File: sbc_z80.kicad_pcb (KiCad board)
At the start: 4 copper layers, 101.6 x 50.8 mm, 72 parts, among them J1 RC80 Bus, J2 UPDI TTL, J3 PIO Header, J4 Conn_01x06, J5 Conn_01x06, J6 CTC Header, J7 AVR-JTAG-10, SW1 SW_Push, SW2 SW_DIP_x06, U1 CPU - Z84C0010AEG, U10 74HC04, U11 ATtiny1614-SS, U12 MIC811LUY, U13 AS1115-BSST, U14 ACDA02-41SGWA-F01, U2 TPS7A0533PDBVR, U3 SRAM - IS62C5128BL-45TLI, U4 GLS29EE010, U5 Si5351A-B-GT, U6 SIO/3 - Z84C4310AEG, U7 CPLD - EPM7032STC44, U8 CTC - Z84C3010AEG, U9 PIO - Z84C2010AEG, Y1 25MHZ 8PF

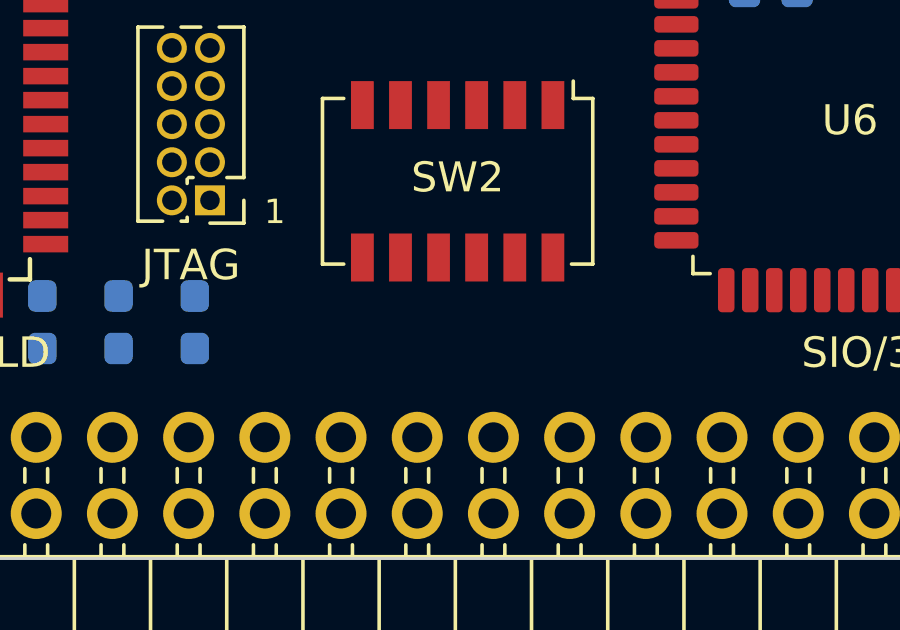
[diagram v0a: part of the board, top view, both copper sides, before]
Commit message: fixed NC pins
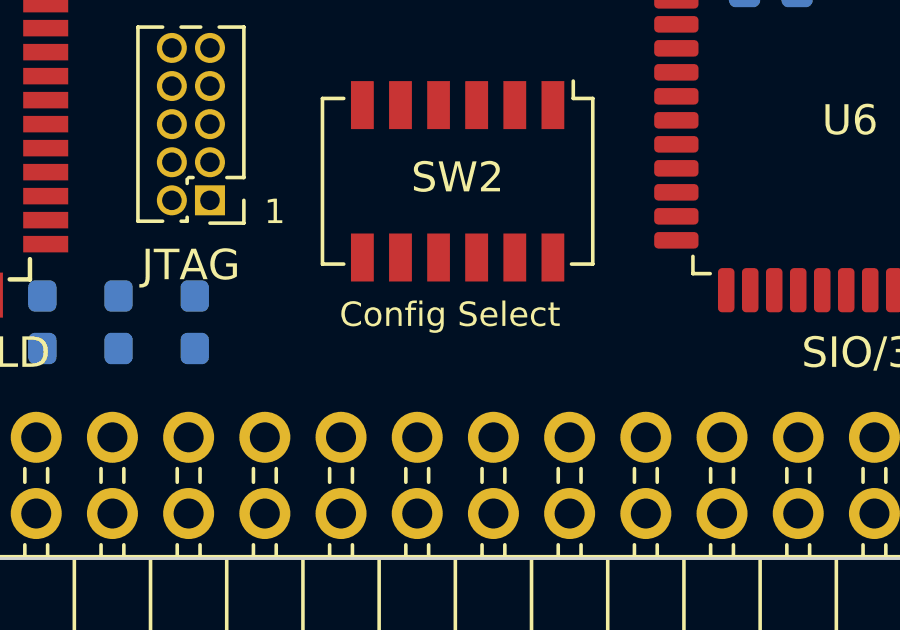
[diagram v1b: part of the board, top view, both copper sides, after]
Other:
- board text added: "Config Select"
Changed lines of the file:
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@@
   (general
     (thickness 1.6)
-    (drawings 37)
+    (drawings 38)
     (tracks 0)
     (zones 0)
@@
     (add_net /A17)
     (add_net /A18)
-    (add_net /A19)
     (add_net /A2)
-    (add_net /A20)
-    (add_net /A21)
-    (add_net /A22)
-    (add_net /A23)
     (add_net /A3)
     (add_net /A4)
@@
     (add_net /BRDY)
     (add_net /CLK)
-    (add_net /CLK2)
-    (add_net /CLKX)
     (add_net /CLK_F)
     (add_net /CLK_U)
@@
     (add_net /D0)
     (add_net /D1)
-    (add_net /D10)
-    (add_net /D11)
-    (add_net /D12)
-    (add_net /D13)
-    (add_net /D14)
-    (add_net /D15)
     (add_net /D2)
     (add_net /D3)
@@
     (add_net /D6)
     (add_net /D7)
-    (add_net /D8)
-    (add_net /D9)
-    (add_net "/Display and Clocks/D_ENA")
     (add_net "/Display and Clocks/RX")
     (add_net "/Display and Clocks/SCL")
@@
     (add_net /TXA)
     (add_net /TXB)
-    (add_net /USR1)
-    (add_net /USR2)
-    (add_net /USR3)
-    (add_net /USR5)
-    (add_net /USR6)
-    (add_net /USR7)
     (add_net /ZT0)
     (add_net /ZT1)
     (add_net /ZT2)
-    (add_net /~A0)
     (add_net /~ASTB)
     (add_net /~BSTB)
@@
     (add_net /~CTSA)
     (add_net /~CTSB)
-    (add_net /~DIO)
     (add_net /~HALT)
     (add_net /~INT)
@@
     (add_net /~MREQ)
     (add_net /~NMI)
-    (add_net /~PAGE)
     (add_net /~PIO)
     (add_net /~RAM)
     (add_net /~RD)
     (add_net /~RESET)
-    (add_net /~RFSH)
     (add_net /~ROM)
     (add_net /~RTSA)
@@
     (add_net "Net-(D1-Pad3)")
     (add_net "Net-(D1-Pad4)")
-    (add_net "Net-(J1-Pad41)")
-    (add_net "Net-(J1-Pad42)")
-    (add_net "Net-(J1-Pad43)")
-    (add_net "Net-(J1-Pad44)")
-    (add_net "Net-(J1-Pad45)")
-    (add_net "Net-(J1-Pad46)")
-    (add_net "Net-(J1-Pad47)")
-    (add_net "Net-(J1-Pad48)")
     (add_net "Net-(J4-Pad2)")
-    (add_net "Net-(J4-Pad3)")
     (add_net "Net-(J4-Pad4)")
     (add_net "Net-(J4-Pad5)")
     (add_net "Net-(J4-Pad6)")
     (add_net "Net-(J5-Pad2)")
-    (add_net "Net-(J5-Pad3)")
     (add_net "Net-(J5-Pad4)")
     (add_net "Net-(J5-Pad5)")
     (add_net "Net-(J5-Pad6)")
-    (add_net "Net-(J7-Pad7)")
-    (add_net "Net-(J7-Pad8)")
     (add_net "Net-(R22-Pad1)")
     (add_net "Net-(R4-Pad2)")
     (add_net "Net-(SW1-Pad2)")
-    (add_net "Net-(SW2-Pad1)")
-    (add_net "Net-(SW2-Pad10)")
-    (add_net "Net-(SW2-Pad11)")
-    (add_net "Net-(SW2-Pad12)")
-    (add_net "Net-(SW2-Pad2)")
-    (add_net "Net-(SW2-Pad3)")
-    (add_net "Net-(SW2-Pad4)")
-    (add_net "Net-(SW2-Pad5)")
-    (add_net "Net-(SW2-Pad6)")
-    (add_net "Net-(SW2-Pad7)")
-    (add_net "Net-(SW2-Pad8)")
-    (add_net "Net-(SW2-Pad9)")
     (add_net "Net-(U1-Pad11)")
-    (add_net "Net-(U1-Pad25)")
     (add_net "Net-(U10-Pad1)")
-    (add_net "Net-(U10-Pad12)")
     (add_net "Net-(U10-Pad3)")
     (add_net "Net-(U10-Pad5)")
-    (add_net "Net-(U13-Pad1)")
-    (add_net "Net-(U13-Pad10)")
-    (add_net "Net-(U13-Pad11)")
-    (add_net "Net-(U13-Pad12)")
-    (add_net "Net-(U13-Pad13)")
-    (add_net "Net-(U13-Pad14)")
-    (add_net "Net-(U13-Pad15)")
-    (add_net "Net-(U13-Pad16)")
-    (add_net "Net-(U13-Pad17)")
-    (add_net "Net-(U13-Pad18)")
-    (add_net "Net-(U13-Pad19)")
-    (add_net "Net-(U13-Pad2)")
-    (add_net "Net-(U13-Pad20)")
-    (add_net "Net-(U13-Pad21)")
-    (add_net "Net-(U13-Pad22)")
-    (add_net "Net-(U13-Pad23)")
-    (add_net "Net-(U13-Pad24)")
-    (add_net "Net-(U13-Pad3)")
-    (add_net "Net-(U13-Pad4)")
-    (add_net "Net-(U13-Pad5)")
-    (add_net "Net-(U13-Pad6)")
-    (add_net "Net-(U13-Pad7)")
-    (add_net "Net-(U13-Pad8)")
-    (add_net "Net-(U13-Pad9)")
-    (add_net "Net-(U14-Pad1)")
-    (add_net "Net-(U14-Pad10)")
-    (add_net "Net-(U14-Pad11)")
-    (add_net "Net-(U14-Pad12)")
-    (add_net "Net-(U14-Pad13)")
-    (add_net "Net-(U14-Pad14)")
-    (add_net "Net-(U14-Pad15)")
-    (add_net "Net-(U14-Pad16)")
-    (add_net "Net-(U14-Pad17)")
-    (add_net "Net-(U14-Pad18)")
-    (add_net "Net-(U14-Pad19)")
-    (add_net "Net-(U14-Pad2)")
-    (add_net "Net-(U14-Pad20)")
-    (add_net "Net-(U14-Pad3)")
-    (add_net "Net-(U14-Pad4)")
-    (add_net "Net-(U14-Pad5)")
-    (add_net "Net-(U14-Pad6)")
-    (add_net "Net-(U14-Pad7)")
-    (add_net "Net-(U14-Pad8)")
-    (add_net "Net-(U14-Pad9)")
-    (add_net "Net-(U2-Pad4)")
     (add_net "Net-(U4-Pad1)")
     (add_net "Net-(U5-Pad2)")
     (add_net "Net-(U5-Pad3)")
-    (add_net "Net-(U6-Pad1)")
-    (add_net "Net-(U6-Pad10)")
-    (add_net "Net-(U6-Pad15)")
-    (add_net "Net-(U6-Pad16)")
     (add_net "Net-(U6-Pad17)")
-    (add_net "Net-(U6-Pad38)")
-    (add_net "Net-(U6-Pad40)")
-    (add_net "Net-(U7-Pad18)")
-    (add_net "Net-(U7-Pad19)")
-    (add_net "Net-(U7-Pad20)")
-    (add_net "Net-(U7-Pad21)")
-    (add_net "Net-(U7-Pad22)")
-    (add_net "Net-(U7-Pad23)")
-    (add_net "Net-(U7-Pad25)")
-    (add_net "Net-(U7-Pad38)")
-    (add_net "Net-(U7-Pad39)")
-    (add_net "Net-(U7-Pad40)")
     (add_net "Net-(U8-Pad11)")
     (add_net "Net-(U9-Pad2)")
@@
     )
   )
+  (gr_text "Config Select" (at 148.971 119.38) (layer F.SilkS)
+    (effects (font (size 0.8128 0.8128) (thickness 0.1524)))
+  )
   (gr_text THS-80 (at 95.504 102.87) (layer F.SilkS)

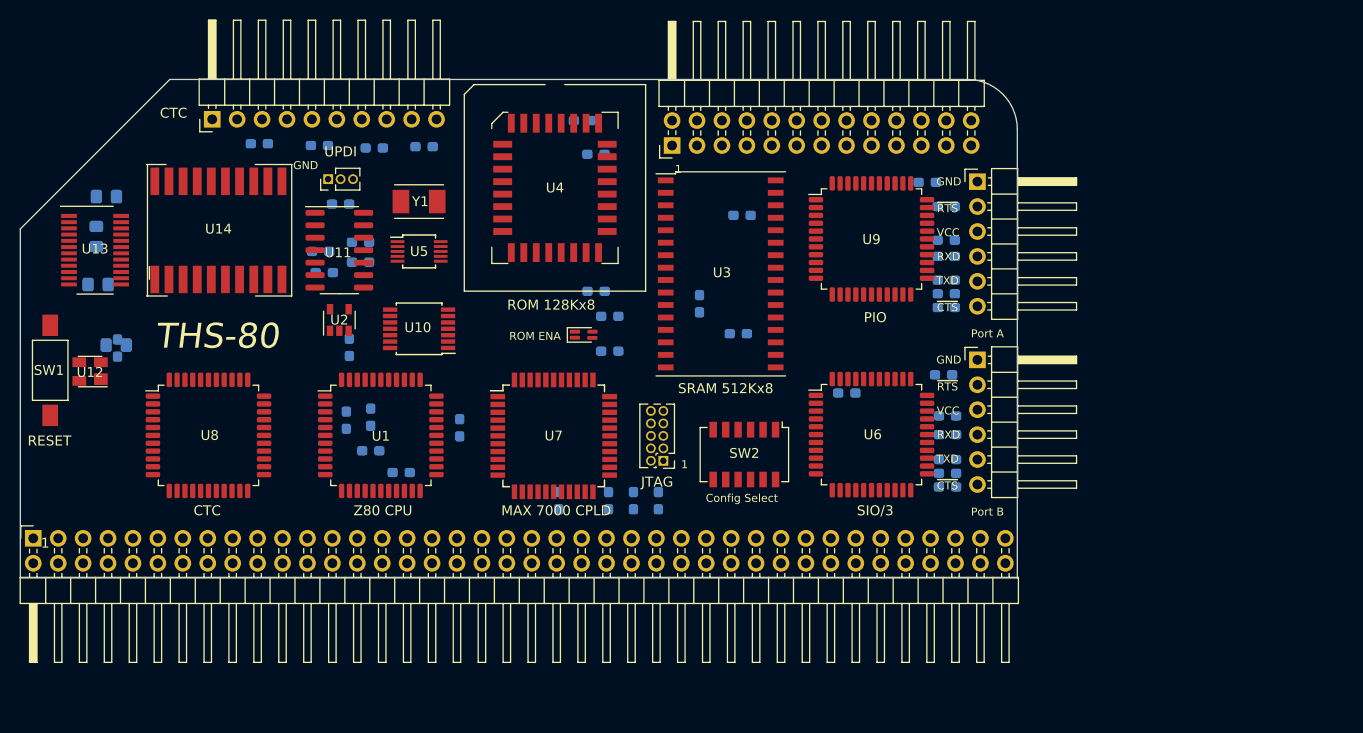
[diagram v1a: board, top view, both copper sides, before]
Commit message: changed part layout, removed switch
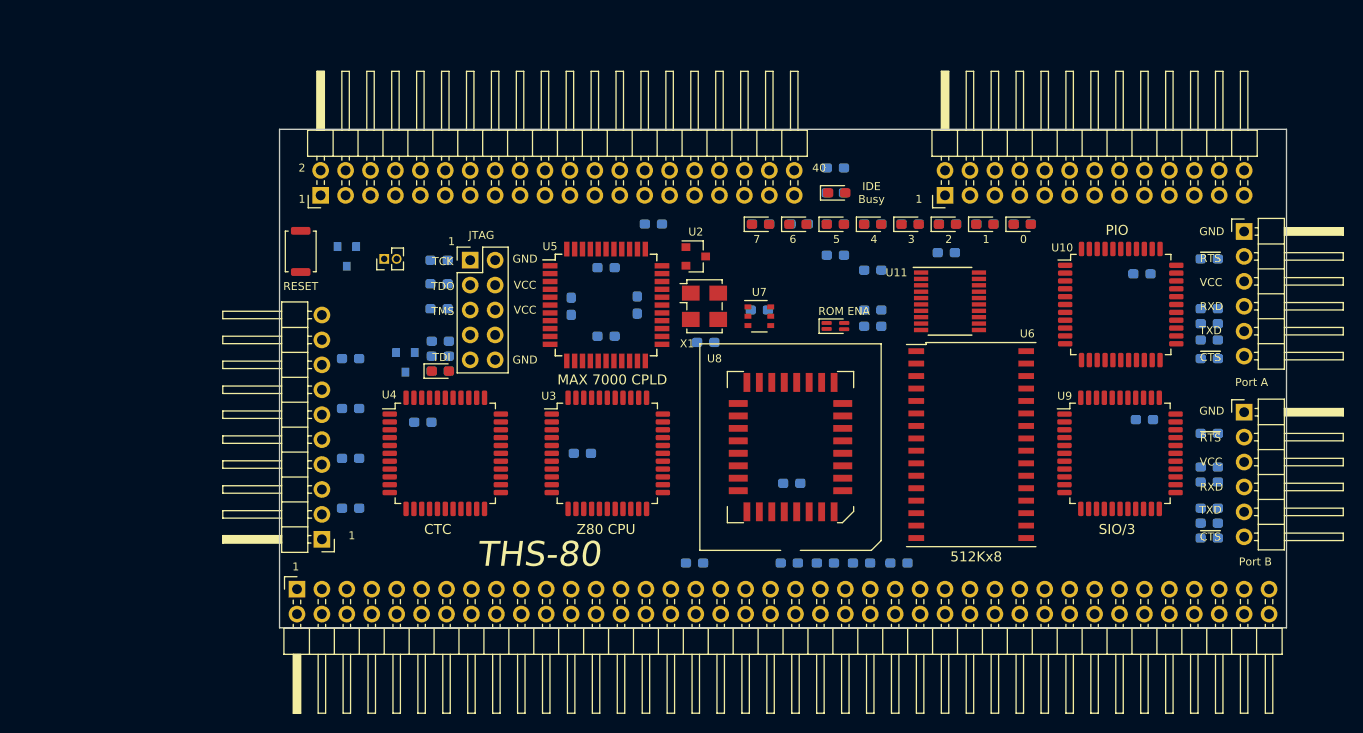
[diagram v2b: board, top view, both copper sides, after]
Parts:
- removed the C1 at (83.2, 92.7)
- removed C15, C16: 0.47uF, Capacitor_SMD:C_0603_1608Metric_Pad1.05x0.95mm_HandSolder
- removed the C2 at (84.2, 88.6)
- removed the C3 at (83.4, 97.6)
- removed the C4 at (85.2, 103.8)
- removed the J5 at (173.0, 105.3)
- removed the R26 at (105.9, 83.4)
- removed the R28 at (116.6, 83.6)
- removed the SW1 at (78.5, 106.3)
- removed U13: AS1115-BSST, Package_SO:QSOP-24_3.9x8.7mm_P0.635mm
- removed U14: ACDA02-41SGWA-F01, Display:ACDA02-41SGWA-F01
- removed the U2 at (108.0, 101.2)
- removed the U4 at (129.9, 87.8)
- removed the U5 at (116.1, 94.2)
- removed Y1: 25MHZ 8PF, Crystal:Crystal_SMD_TXC_7A-2Pin_5x3.2mm
- added C11: 100nF, Capacitor_SMD:C_0603_1608Metric_Pad1.05x0.95mm_HandSolder, B.Cu at (144.1, 126.0)
- added D10: Green, LED_SMD:LED_0603_1608Metric_Pad1.05x0.95mm_HandSolder, F.Cu at (154.7, 91.5)
- added D11: Green, LED_SMD:LED_0603_1608Metric_Pad1.05x0.95mm_HandSolder, F.Cu at (150.9, 91.5)
- added D2: LED, LED_SMD:LED_0603_1608Metric_Pad1.05x0.95mm_HandSolder, F.Cu at (158.6, 88.3)
- added D3: Red/Green, LED_SMD:LED_2C_0603_1608Metric_Pad1.05x0.95mm_HandSolder, F.Cu at (158.5, 101.9)
- added D4: Green, LED_SMD:LED_0603_1608Metric_Pad1.05x0.95mm_HandSolder, F.Cu at (177.5, 91.5)
- added D5: Green, LED_SMD:LED_0603_1608Metric_Pad1.05x0.95mm_HandSolder, F.Cu at (173.7, 91.5)
- added D6: Green, LED_SMD:LED_0603_1608Metric_Pad1.05x0.95mm_HandSolder, F.Cu at (169.9, 91.5)
- added D7: Green, LED_SMD:LED_0603_1608Metric_Pad1.05x0.95mm_HandSolder, F.Cu at (166.1, 91.5)
- added D8: Green, LED_SMD:LED_0603_1608Metric_Pad1.05x0.95mm_HandSolder, F.Cu at (162.3, 91.5)
- added D9: Green, LED_SMD:LED_0603_1608Metric_Pad1.05x0.95mm_HandSolder, F.Cu at (158.5, 91.5)
- added J3: AVR-JTAG-10, Connector_PinHeader_2.54mm:PinHeader_2x05_P2.54mm_Vertical, F.Cu at (121.3, 95.1)
- added JP1: Jumper_NC_Small, Connector_PinHeader_1.27mm:PinHeader_1x02_P1.27mm_Vertical, F.Cu at (112.5, 95.0)
- added Q1: IRLML6402, Package_TO_SOT_SMD:SOT-23, B.Cu at (114.7, 105.5)
- added R29: 680R, Resistor_SMD:R_0603_1608Metric_Pad1.05x0.95mm_HandSolder, B.Cu at (154.8, 91.4)
- added R30: 680R, Resistor_SMD:R_0603_1608Metric_Pad1.05x0.95mm_HandSolder, B.Cu at (150.9, 91.4)
- added R35: 2K2, Resistor_SMD:R_0603_1608Metric_Pad1.05x0.95mm_HandSolder, B.Cu at (196.6, 112.8)
- added R36: 2K2, Resistor_SMD:R_0603_1608Metric_Pad1.05x0.95mm_HandSolder, B.Cu at (196.6, 117.7)
- added R37: 2K2, Resistor_SMD:R_0603_1608Metric_Pad1.05x0.95mm_HandSolder, B.Cu at (196.6, 120.4)
- added R38: 2K2, Resistor_SMD:R_0603_1608Metric_Pad1.05x0.95mm_HandSolder, B.Cu at (196.6, 123.4)
- added R39: 100K, Resistor_SMD:R_0603_1608Metric_Pad1.05x0.95mm_HandSolder, B.Cu at (196.6, 101.6)
- added R40: 100K, Resistor_SMD:R_0603_1608Metric_Pad1.05x0.95mm_HandSolder, B.Cu at (196.6, 116.2)
- added R41: 100K, Resistor_SMD:R_0603_1608Metric_Pad1.05x0.95mm_HandSolder, B.Cu at (162.3, 96.1)
- added R42: 100K, Resistor_SMD:R_0603_1608Metric_Pad1.05x0.95mm_HandSolder, B.Cu at (196.6, 121.9)
- added R6: 10K, Resistor_SMD:R_0603_1608Metric_Pad1.05x0.95mm_HandSolder, B.Cu at (109.1, 115.3)
- added R7: 10K, Resistor_SMD:R_0603_1608Metric_Pad1.05x0.95mm_HandSolder, B.Cu at (109.1, 110.2)
- added R8: 10K, Resistor_SMD:R_0603_1608Metric_Pad1.05x0.95mm_HandSolder, B.Cu at (109.1, 105.2)
- added R9: 10K, Resistor_SMD:R_0603_1608Metric_Pad1.05x0.95mm_HandSolder, B.Cu at (109.1, 120.4)
- added U10: Z84C2010AEG, Package_QFP:LQFP-44_10x10mm_P0.8mm, F.Cu at (187.6, 99.6)
- added U6: SRAM - IS62C5128BL-45TLI, Package_SO:TSOP-II-32_21.0x10.2mm_P1.27mm, F.Cu at (172.3, 113.9)
- added X1: CTX-636 50mhz, Oscillator:Oscillator_SMD_TXC_7C-4Pin_5.0x3.2mm_HandSoldering, F.Cu at (145.2, 99.8)
- C7: renamed from C11; value 100nF -> 2.2uF
- D1: value Red/Green -> Green; footprint LED_SMD:LED_2C_0603_1608Metric_Pad1.05x0.95mm_HandSolder -> LED_SMD:LED_0603_1608Metric_Pad1.05x0.95mm_HandSolder
- J1: renamed from J4; value Conn_01x06 -> RC80 Bus; footprint Connector_PinHeader_2.54mm:PinHeader_1x06_P2.54mm_Horizontal -> Connector_PinHeader_2.54mm:PinHeader_2x40_Top_Bottom_P2.54mm_Horizontal
- J2: value UPDI TTL -> CTC Header; footprint Connector_PinHeader_1.27mm:PinHeader_1x03_P1.27mm_Vertical -> Connector_PinHeader_2.54mm:PinHeader_1x10_P2.54mm_Horizontal
- J4: renamed from J1; value RC80 Bus -> IDE; footprint Connector_PinHeader_2.54mm:PinHeader_2x40_Top_Bottom_P2.54mm_Horizontal -> Connector_PinHeader_2.54mm:PinHeader_2x20_P2.54mm_Horizontal
- J6: value CTC Header -> Conn_01x06; footprint Connector_PinHeader_2.54mm:PinHeader_1x10_P2.54mm_Horizontal -> Connector_PinHeader_2.54mm:PinHeader_1x06_P2.54mm_Horizontal
- J7: value AVR-JTAG-10 -> Conn_01x06; footprint Connector_PinHeader_1.27mm:PinHeader_2x05_P1.27mm_Vertical -> Connector_PinHeader_2.54mm:PinHeader_1x06_P2.54mm_Horizontal
- R1: renamed from R9; value 100K -> 10K
- R10, R16: value 2K2 -> 1K
- R11, R12, R18: value 2K2 -> 10K
- R13: value 2K2 -> 100R
- R14, R15: value 100K -> 10K
- R17: value 2K2 -> 360R
- R19: value 2K2 -> 680R
- R20: value 100K -> 680R
- R21: value 1K -> 10K
- R23, R24, R27: value 10K -> 680R
- R25: renamed from R4; value 10K -> 680R
- R28: renamed from R25; value 10K -> 680R
- R3: renamed from R8; value 10K -> 100R
- R31: renamed from R30; value 680R -> 2K2
- R32: renamed from R1; value 1K -> 2K2
- R33: renamed from R2; value 1K -> 2K2
- R34: renamed from R3; value 4K7 -> 2K2
- SW1: renamed from SW2; value SW_DIP_x06 -> Reset; footprint Button_Switch_SMD:SW_DIP_SPSTx06_Slide_Copal_CHS-06A_W5.08mm_P1.27mm_JPin -> Button_Switch_SMD:SW_Push_SPST_NO_Alps_SKRK
- U1: renamed from U6; value SIO/3 - Z84C4310AEG -> DS1813R-5+T&R; footprint Package_QFP:LQFP-44_10x10mm_P0.8mm -> Package_TO_SOT_SMD:SOT-23; moved to B.Cu
- U11: value ATtiny1614-SS -> 74HCT273; footprint Package_SO:SOIC-14_3.9x8.7mm_P1.27mm -> Package_SO:TSSOP-20_4.4x6.5mm_P0.65mm
- U2: renamed from U7; value CPLD - EPM7032STC44 -> AP7381-33SA; footprint Package_QFP:TQFP-44_10x10mm_P0.8mm -> Package_TO_SOT_SMD:SOT-23
- U3: renamed from U1; value CPU - Z84C0010AEG -> CPU -Z84C0020AEG
- U4: renamed from U9; value PIO - Z84C2010AEG -> CTC - Z84C3010AEG
- U5: renamed from U3; value SRAM - IS62C5128BL-45TLI -> CPLD - EPM7032STC44; footprint Package_SO:TSOP-II-32_21.0x10.2mm_P1.27mm -> Package_QFP:TQFP-44_10x10mm_P0.8mm
- U7: renamed from U12; value MIC811LUY -> 74HCT2G04; footprint Package_TO_SOT_SMD:SOT-143 -> Package_SO:TSOP-6_1.65x3.05mm_P0.95mm
- U8: renamed from U10; value 74HC04 -> SST39SF040; footprint Package_SO:TSSOP-14_4.4x5mm_P0.65mm -> Package_LCC:PLCC-32_SMD-Socket
- U9: renamed from U8; value CTC - Z84C3010AEG -> SIO/3 - Z84C4310AEG
- moved J6 105.8 mm to (200.2, 92.2), turned to 0 degrees
- moved U9 92.9 mm to (187.5, 114.8)
- moved R34 89.9 mm to (196.6, 105.2)
- moved R33 86.8 mm to (196.6, 103.3), turned to 180 degrees
- moved R32 86.8 mm to (196.6, 100.1), turned to 180 degrees
- moved J1 83.6 mm to (103.6, 133.7), turned to 90 degrees
- moved R23 70.3 mm to (177.5, 91.4)
- moved U7 68.4 mm to (150.7, 100.8), turned to 0 degrees
- moved R24 66.0 mm to (173.7, 91.4), turned to 0 degrees
- moved U11 62.4 mm to (170.2, 99.3)
- moved R31 61.8 mm to (196.6, 95.0)
- moved J7 59.4 mm to (200.2, 110.6), turned to 0 degrees
- moved R28 59.3 mm to (158.5, 91.4), turned to 0 degrees
- moved U1 56.5 mm to (108.7, 94.7), turned to 270 degrees
- moved R15 52.6 mm to (118.2, 103.4)
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- renumbered C5 to C1, C14 to C10, C6 to C2, C7 to C3, C8 to C4, C9 to C5, C10 to C6, C12 to C8, C13 to C9, J3 to J5, R5 to R2, R29 to R26, R7 to R4, R6 to R5
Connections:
- C1 pad 1: Net-(C10-Pad1) -> VCC
- C10 pad 1: Net-(C10-Pad1) -> VCC
- C2 pad 1: Net-(C10-Pad1) -> VCC
- C3 pad 1: Net-(C10-Pad1) -> VCC
- C4 pad 1: Net-(C10-Pad1) -> VCC
- C5 pad 1: Net-(C10-Pad1) -> VCC
- C6 pad 1: Net-(C10-Pad1) -> VCC
- C7 pad 1: Net-(C10-Pad1) -> /3V3
- C8 pad 1: Net-(C10-Pad1) -> VCC
- C9 pad 1: Net-(C10-Pad1) -> VCC
- J1 pad 1: GND -> /A15
- J1 pad 2: Net-(J4-Pad2) -> /A14
- J1 pad 3: (no net) -> /A13
- J1 pad 4: Net-(J4-Pad4) -> /A12
- J1 pad 5: Net-(J4-Pad5) -> /A11
- J1 pad 6: Net-(J4-Pad6) -> /A10
- J2 pad 1: GND -> VCC
- J2 pad 2: /Display and Clocks/TX -> /CLK_U
- J2 pad 3: /Display and Clocks/RX -> /ZT0
- J4 pad 1: /A15 -> /~RESET
- J4 pad 10: /A6 -> (no net)
- J4 pad 11: /A5 -> /D3
- J4 pad 12: /A4 -> (no net)
- J4 pad 13: /A3 -> /D2
- J4 pad 14: /A2 -> (no net)
- J4 pad 15: /A1 -> /D1
- J4 pad 16: /A0 -> (no net)
- J4 pad 17: GND -> /D0
- J4 pad 18: +5V -> (no net)
- J4 pad 19: /~M1 -> GND
- J4 pad 2: /A14 -> GND
- J4 pad 20: /~RESET -> Net-(J7-Pad20)
- J4 pad 21: /CLK -> (no net)
- J4 pad 22: /~INT -> GND
- J4 pad 23: /~MREQ -> /~WR
- J4 pad 24: /~WR -> GND
- J4 pad 26: /~IORQ -> GND
- J4 pad 27: /D0 -> (no net)
- J4 pad 28: /D1 -> (no net)
- J4 pad 29: /D2 -> Net-(J7-Pad29)
- J4 pad 3: /A13 -> /D7
- J4 pad 30: /D3 -> GND
- J4 pad 31: /D4 -> (no net)
- J4 pad 32: /D5 -> (no net)
- J4 pad 33: /D6 -> /A1
- J4 pad 34: /D7 -> Net-(J7-Pad34)
- J4 pad 35: /TXA -> /A0
- J4 pad 36: /RXA -> /A2
- J4 pad 37: (no net) -> /~CF
- J4 pad 38: (no net) -> Net-(J7-Pad38)
- J4 pad 39: (no net) -> /~ACTIVE
- J4 pad 4: /A12 -> (no net)
- J4 pad 40: /IEO -> GND
- J4 pad 5: /A11 -> /D6
- J4 pad 6: /A10 -> (no net)
- J4 pad 7: /A9 -> /D5
- J4 pad 8: /A8 -> (no net)
- J4 pad 9: /A7 -> /D4
- J5 pad 1: +5V -> VCC
- J5 pad 10: /PB2 -> /PB5
- J5 pad 11: /PA4 -> /PA3
- J5 pad 12: /PB3 -> /PB4
- J5 pad 13: /PA5 -> /PA2
- J5 pad 14: /PB4 -> /PB3
- J5 pad 15: /PA6 -> /PA1
- J5 pad 16: /PB5 -> /PB2
- J5 pad 17: /PA7 -> /PA0
- J5 pad 18: /PB6 -> /PB1
- J5 pad 20: /PB7 -> /PB0
- J5 pad 26: +5V -> VCC
- J5 pad 3: /PA0 -> /PA7
- J5 pad 5: /PA1 -> /PA6
- J5 pad 6: /PB0 -> /PB7
- J5 pad 7: /PA2 -> /PA5
- J5 pad 8: /PB1 -> /PB6
- J5 pad 9: /PA3 -> /PA4
- J6 pad 1: +5V -> GND
- J6 pad 2: /CT0 -> Net-(J1-Pad2)
- J6 pad 3: /ZT0 -> (no net)
- J6 pad 4: /CT1 -> Net-(J1-Pad4)
- J6 pad 5: /ZT1 -> Net-(J1-Pad5)
- J6 pad 6: /CT2 -> Net-(J1-Pad6)
- J7 pad 1: /TCK -> GND
- J7 pad 2: GND -> Net-(J3-Pad2)
- J7 pad 3: /TDO -> (no net)
- J7 pad 4: +5V -> Net-(J3-Pad4)
- J7 pad 5: /TMS -> Net-(J3-Pad5)
- J7 pad 6: +5V -> Net-(J3-Pad6)
- R1 pad 1: +5V -> VCC
- R1 pad 2: Net-(J4-Pad4) -> /~INT
- R10 pad 1: Net-(J4-Pad2) -> GND
- R10 pad 2: /~RTSA -> /TCK
- R11 pad 1: Net-(J4-Pad4) -> VCC
- R11 pad 2: /RXA -> Net-(R27-Pad2)
- R12 pad 1: Net-(J4-Pad5) -> VCC
- R12 pad 2: /TXA -> /TMS
- R13 pad 1: Net-(J4-Pad6) -> Net-(Q1-Pad1)
- R13 pad 2: /~CTSA -> /TDI
- R14 pad 1: Net-(J4-Pad6) -> VCC
- R14 pad 2: GND -> /TDO
- R15 pad 1: +5V -> VCC
- R15 pad 2: Net-(J5-Pad4) -> /TDI
- R16 pad 1: Net-(J5-Pad2) -> VCC
- R16 pad 2: /~RTSB -> Net-(D3-Pad2)
- R17 pad 1: Net-(J5-Pad4) -> Net-(D1-Pad1)
- R17 pad 2: /RXB -> GND
- R18 pad 1: Net-(J5-Pad5) -> VCC
- R18 pad 2: /TXB -> Net-(J7-Pad29)
- R19 pad 1: Net-(J5-Pad6) -> Net-(D2-Pad1)
- R19 pad 2: /~CTSB -> VCC
- R2 pad 1: /~INT -> VCC
- R2 pad 2: +5V -> /~NMI
- R20 pad 1: Net-(J5-Pad6) -> Net-(D2-Pad3)
- R20 pad 2: GND -> VCC
- R21 pad 1: GND -> VCC
- R21 pad 2: /TCK -> Net-(J7-Pad38)
- R22 pad 1: Net-(R22-Pad1) -> VCC
- R22 pad 2: /TMS -> Net-(J7-Pad34)
- R23 pad 1: Net-(R22-Pad1) -> Net-(R10-Pad1)
- R23 pad 2: /TDO -> Net-(D4-Pad2)
- R24 pad 1: Net-(R22-Pad1) -> Net-(R38-Pad1)
- R24 pad 2: /TDI -> Net-(D5-Pad2)
- R25 pad 1: +5V -> Net-(R39-Pad1)
- R26 pad 1: Net-(D1-Pad1) -> Net-(R40-Pad1)
- R26 pad 2: +5V -> Net-(D7-Pad2)
- R27 pad 1: /CT2 -> Net-(R41-Pad1)
- R27 pad 2: +5V -> Net-(D8-Pad2)
- R28 pad 1: /CT0 -> Net-(R42-Pad1)
- R28 pad 2: +5V -> Net-(D9-Pad2)
- R3 pad 1: /~BUSREQ -> Net-(R7-Pad1)
- R3 pad 2: +5V -> /CLK_50
- R31 pad 1: Net-(D1-Pad3) -> Net-(J1-Pad2)
- R31 pad 2: +5V -> /~RTSA
- R32 pad 1: +3V3 -> Net-(J1-Pad4)
- R32 pad 2: /Display and Clocks/SCL -> /RXA
- R33 pad 1: +3V3 -> Net-(J1-Pad5)
- R33 pad 2: /Display and Clocks/SDA -> /TXA
- R34 pad 1: /Display and Clocks/TX -> Net-(J1-Pad6)
- R34 pad 2: /Display and Clocks/RX -> /~CTSA
- R4 pad 1: /~WAIT -> VCC
- R4 pad 2: +5V -> /~WAIT
- R5 pad 1: /~NMI -> VCC
- R5 pad 2: +5V -> /~BUSREQ
- SW1 pad 1: (no net) -> /~RESET
- SW1 pad 2: (no net) -> GND
- U1 pad 1: (no net) -> /~RESET
- U1 pad 2: /~RTSA -> VCC
- U1 pad 3: /~CTSA -> GND
- U11 pad 1: +3V3 -> /~RESET
- U11 pad 10: /Display and Clocks/RX -> GND
- U11 pad 11: /D0 -> /D_LED
- U11 pad 12: /D1 -> Net-(R41-Pad1)
- U11 pad 13: /D2 -> /D4
- U11 pad 14: GND -> /D5
- U11 pad 2: /D3 -> Net-(R10-Pad1)
- U11 pad 3: /D4 -> /D0
- U11 pad 4: /D5 -> /D1
- U11 pad 5: /D6 -> Net-(R38-Pad1)
- U11 pad 6: (no net) -> Net-(R39-Pad1)
- U11 pad 7: /D7 -> /D2
- U11 pad 8: /Display and Clocks/SDA -> /D3
- U11 pad 9: /Display and Clocks/SCL -> Net-(R40-Pad1)
- U2 pad 1: /TDI -> VCC
- U2 pad 2: /A5 -> GND
- U2 pad 3: /A6 -> /3V3
- U3 pad 11: Net-(U1-Pad11) -> (no net)
- U3 pad 17: Net-(U1-Pad11) -> (no net)
- U3 pad 25: (no net) -> /~RFSH
- U3 pad 33: Net-(U1-Pad11) -> (no net)
- U3 pad 39: Net-(U1-Pad11) -> (no net)
- U3 pad 6: +5V -> VCC
- U4 pad 1: /~IORQ -> /D0
- U4 pad 10: /~PIO -> /D6
- U4 pad 11: /A1 -> (no net)
- U4 pad 12: /A0 -> /D7
- U4 pad 13: /PA7 -> GND
- U4 pad 14: /PA6 -> /~RD
- U4 pad 15: /PA5 -> (no net)
- U4 pad 16: /PA4 -> /ZT0
- U4 pad 18: GND -> /ZT1
- U4 pad 19: /PA3 -> /ZT2
- U4 pad 2: Net-(U9-Pad2) -> /D1
- U4 pad 20: /PA2 -> (no net)
- U4 pad 21: /PA1 -> /~IORQ
- U4 pad 22: /PA0 -> /IEO
- U4 pad 23: /~ASTB -> /~INT
- U4 pad 24: /~BSTB -> (no net)
- U4 pad 25: /ARDY -> /IEI
- U4 pad 26: /D0 -> (no net)
- U4 pad 27: /D1 -> /~M1
- U4 pad 28: Net-(U9-Pad2) -> (no net)
- U4 pad 29: /BRDY -> /CLK_CPU
- U4 pad 3: /~M1 -> /D2
- U4 pad 30: /IEO -> (no net)
- U4 pad 31: /~INT -> /~SIO
- U4 pad 32: /IEI -> /~RESET
- U4 pad 33: /CLK -> /A0
- U4 pad 34: +5V -> (no net)
- U4 pad 35: /PB0 -> /A1
- U4 pad 36: /PB1 -> /CLK_U
- U4 pad 37: /PB2 -> /CLK_U
- U4 pad 38: /PB3 -> (no net)
- U4 pad 39: Net-(U9-Pad2) -> (no net)
- U4 pad 4: /D5 -> /D3
- U4 pad 40: /PB4 -> /CLK_U
- U4 pad 41: /PB5 -> /CLK_U
- U4 pad 42: /PB6 -> (no net)
- U4 pad 43: /PB7 -> VCC
- U4 pad 44: /~RD -> (no net)
- U4 pad 5: /D4 -> (no net)
- U4 pad 6: /D3 -> (no net)
- U4 pad 7: /D2 -> (no net)
- U4 pad 8: /D7 -> /D4
- U4 pad 9: /D6 -> /D5
- U5 pad 1: /A17 -> /TDI
- U5 pad 10: /A2 -> /A15
- U5 pad 11: /A1 -> /D0
- U5 pad 12: /A0 -> /D7
- U5 pad 13: /D0 -> /~M1
- U5 pad 14: /D1 -> /~RD
- U5 pad 15: /D2 -> /~WR
- U5 pad 17: /D3 -> VCC
- U5 pad 18: /D4 -> /CLK_U
- U5 pad 19: /D5 -> /CLK_CPU
- U5 pad 2: /A16 -> /A3
- U5 pad 20: /D6 -> (no net)
- U5 pad 21: /D7 -> /D_LED
- U5 pad 22: /~RAM -> (no net)
- U5 pad 23: /A10 -> (no net)
- U5 pad 24: /~RD -> GND
- U5 pad 25: /A11 -> /A16
- U5 pad 26: /A9 -> /TCK
- U5 pad 27: /A8 -> /~PAGE
- U5 pad 28: /A13 -> /~CF
- U5 pad 29: /~WR -> VCC
- U5 pad 3: /A14 -> /A4
- U5 pad 30: /A18 -> /~PIO
- U5 pad 31: /A15 -> (no net)
- U5 pad 32: +5V -> /TDO
- U5 pad 4: /A12 -> GND
- U5 pad 5: /A7 -> /A5
- U5 pad 7: /A5 -> /TMS
- U5 pad 8: /A4 -> /A7
- U5 pad 9: /A3 -> VCC
- U7 pad 1: GND -> /~ROM
- U7 pad 2: /~RESET -> GND
- U7 pad 3: Net-(SW1-Pad2) -> Net-(D2-Pad2)
- U7 pad 4: +5V -> Net-(D2-Pad4)
- U8 pad 1: Net-(U10-Pad1) -> /A18
- U8 pad 10: Net-(D1-Pad2) -> /A2
- U8 pad 11: /~ROM -> /A1
- U8 pad 12: (no net) -> /A0
- U8 pad 13: GND -> /D0
- U8 pad 14: +5V -> /D1
- U8 pad 2: /CLK_F -> /A16
- U8 pad 3: Net-(U10-Pad3) -> /A15
- U8 pad 4: /CLK -> /A12
- U8 pad 5: Net-(U10-Pad5) -> /A7
- U8 pad 6: /CLK_U -> /A6
- U8 pad 7: GND -> /A5
- U8 pad 8: Net-(D1-Pad4) -> /A4
- U8 pad 9: Net-(D1-Pad2) -> /A3
- U9 pad 1: /D0 -> (no net)
- U9 pad 10: /D6 -> (no net)
- U9 pad 11: Net-(U8-Pad11) -> /TXB
- U9 pad 12: /D7 -> /CLK_U
- U9 pad 13: GND -> /CLK_U
- U9 pad 14: /~RD -> /RXB
- U9 pad 15: Net-(U8-Pad11) -> (no net)
- U9 pad 16: /ZT0 -> (no net)
- U9 pad 17: Net-(U8-Pad11) -> (no net)
- U9 pad 18: /ZT1 -> GND
- U9 pad 19: /ZT2 -> /~RD
- U9 pad 2: /D1 -> /~RTSA
- U9 pad 20: Net-(U8-Pad11) -> /A0
- U9 pad 21: /~IORQ -> /A1
- U9 pad 22: /IEI -> /~SIO
- U9 pad 23: /IEO -> /~IORQ
- U9 pad 24: Net-(U8-Pad11) -> /D6
- U9 pad 25: /~INT -> /D4
- U9 pad 26: Net-(U8-Pad11) -> /D2
- U9 pad 27: /~M1 -> (no net)
- U9 pad 28: Net-(U8-Pad11) -> (no net)
- U9 pad 29: /CLK -> /D1
- U9 pad 3: /D2 -> /~CTSA
- U9 pad 30: Net-(U8-Pad11) -> /D3
- U9 pad 31: /~CTC -> /D5
- U9 pad 32: /~RESET -> /D7
- U9 pad 33: /A0 -> /~INT
- U9 pad 34: Net-(U8-Pad11) -> /IEI
- U9 pad 35: /A1 -> /IEO
- U9 pad 36: /CT3 -> /~M1
- U9 pad 37: /CT2 -> VCC
- U9 pad 38: Net-(U8-Pad11) -> (no net)
- U9 pad 39: Net-(U8-Pad11) -> (no net)
- U9 pad 4: /D3 -> GND
- U9 pad 40: /CT1 -> (no net)
- U9 pad 41: /CT0 -> /RXA
- U9 pad 42: Net-(U8-Pad11) -> /CLK_U
- U9 pad 43: +5V -> /CLK_U
- U9 pad 44: Net-(U8-Pad11) -> /TXA
- U9 pad 5: Net-(U8-Pad11) -> /CLK_CPU
- U9 pad 6: Net-(U8-Pad11) -> /~RESET
- U9 pad 7: Net-(U8-Pad11) -> GND
- U9 pad 8: /D4 -> /~CTSB
- U9 pad 9: /D5 -> /~RTSB
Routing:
- added copper zone on In2.Cu, net VCC
- removed copper zone on In2.Cu, net +3V3
- removed copper zone on In2.Cu, net +5V
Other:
- board size 101.6 x 50.8 mm -> 102.6 x 50.8 mm
- board text added: "0"
- board text added: "2"
- board text added: "3"
- board text added: "4"
- board text added: "40"
- board text added: "5"
- board text added: "512Kx8"
- board text added: "6"
- board text added: "7"
- board text added: "IDE Busy"
- board text added: "TCK"
- board text added: "TDI"
- board text added: "TDO"
- board text added: "TMS"
- board text removed: "Config Select"
- board text removed: "ROM 128Kx8"
- board text removed: "SRAM 512Kx8"
- board text removed: "UPDI"

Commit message: added USB power, fixed layout
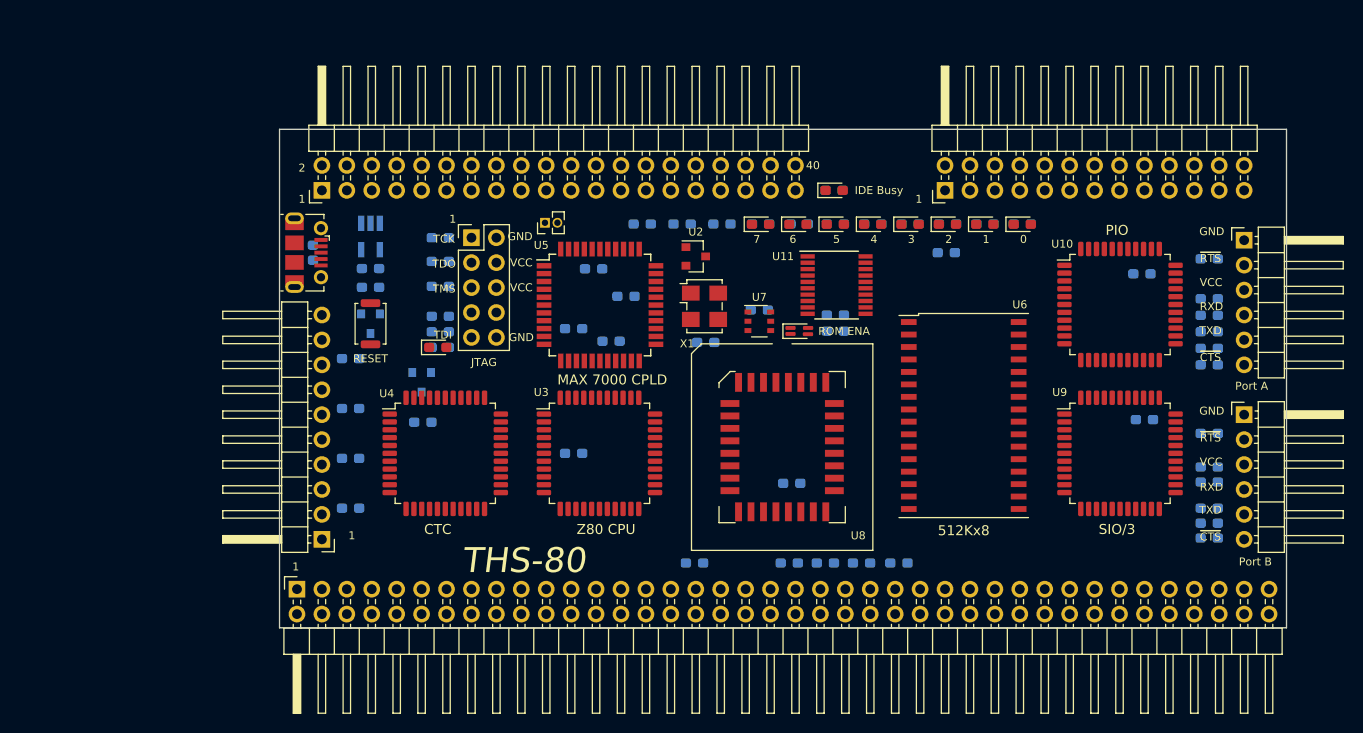
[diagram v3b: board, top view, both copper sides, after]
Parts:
- added C12: 100nF, Capacitor_SMD:C_0603_1608Metric_Pad1.05x0.95mm_HandSolder, B.Cu at (104.4, 95.1)
- added C13: 10uF, Capacitor_SMD:C_0603_1608Metric_Pad1.05x0.95mm_HandSolder, B.Cu at (111.1, 96.0)
- added C14: 1uF, Capacitor_SMD:C_0603_1608Metric_Pad1.05x0.95mm_HandSolder, B.Cu at (111.1, 97.9)
- added J8: USB_B_Micro, Connector_USB:USB_Micro-B_Molex-105017-0001, F.Cu at (104.6, 94.4)
- added R43: 1M, Resistor_SMD:R_0603_1608Metric_Pad1.05x0.95mm_HandSolder, B.Cu at (104.4, 93.6)
- added U12: MAX40200AUK, Package_TO_SOT_SMD:SOT-23-5_HandSoldering, B.Cu at (111.1, 92.7)
- moved R41 35.6 mm to (196.6, 105.8), turned to 180 degrees
- moved JP1 16.8 mm to (128.9, 91.3)
- moved R22 15.9 mm to (142.9, 91.4)
- moved R21 12.9 mm to (146.9, 91.4), turned to 0 degrees
- moved U11 11.7 mm to (158.6, 97.7)
- moved SW1 10.2 mm to (111.1, 101.6)
- moved U1 7.27 mm to (111.1, 101.6)
- moved R19 3.84 mm to (158.5, 100.7)
- moved R20 3.84 mm to (158.5, 102.4)
- moved D3 3.72 mm to (154.8, 102.4)
- moved U6 3.06 mm to (171.6, 111.0)
- moved Q1 2.62 mm to (116.3, 107.6)
- moved R15 2.54 mm to (118.2, 100.8)
- moved R13 2.48 mm to (118.2, 102.4)
- moved D1 2.43 mm to (118.0, 104.0)
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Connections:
- U5 pad 21: /D_LED -> (no net)
- U5 pad 23: (no net) -> /A16
- U5 pad 25: /A16 -> /D_LED

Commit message: routing
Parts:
- added C15: 100nF, Capacitor_SMD:C_0603_1608Metric_Pad1.05x0.95mm_HandSolder, B.Cu at (190.0, 111.6)
- added C16: 100nF, Capacitor_SMD:C_0603_1608Metric_Pad1.05x0.95mm_HandSolder, B.Cu at (158.5, 94.9)
- J6: value Conn_01x06 -> Port A
- J7: value Conn_01x06 -> Port B
- moved C7 46.0 mm to (145.3, 100.3), turned to 180 degrees
- moved C10 8.02 mm to (173.7, 101.3)
- moved R4 0.08 mm to (161.2, 126.0)
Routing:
- added copper zone on B.Cu, net GND
- added copper zone on F.Cu, net GND
- added copper zone on In1.Cu, net GND
